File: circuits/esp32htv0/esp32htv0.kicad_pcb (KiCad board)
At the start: 2 copper layers, 60.5 x 69.3 mm, 39 parts, among them J1 Power, SW1 SW_Push, U1 LD1117S33TR_SOT223, U2 ESP32-WROOM-32UE, U3 BME280

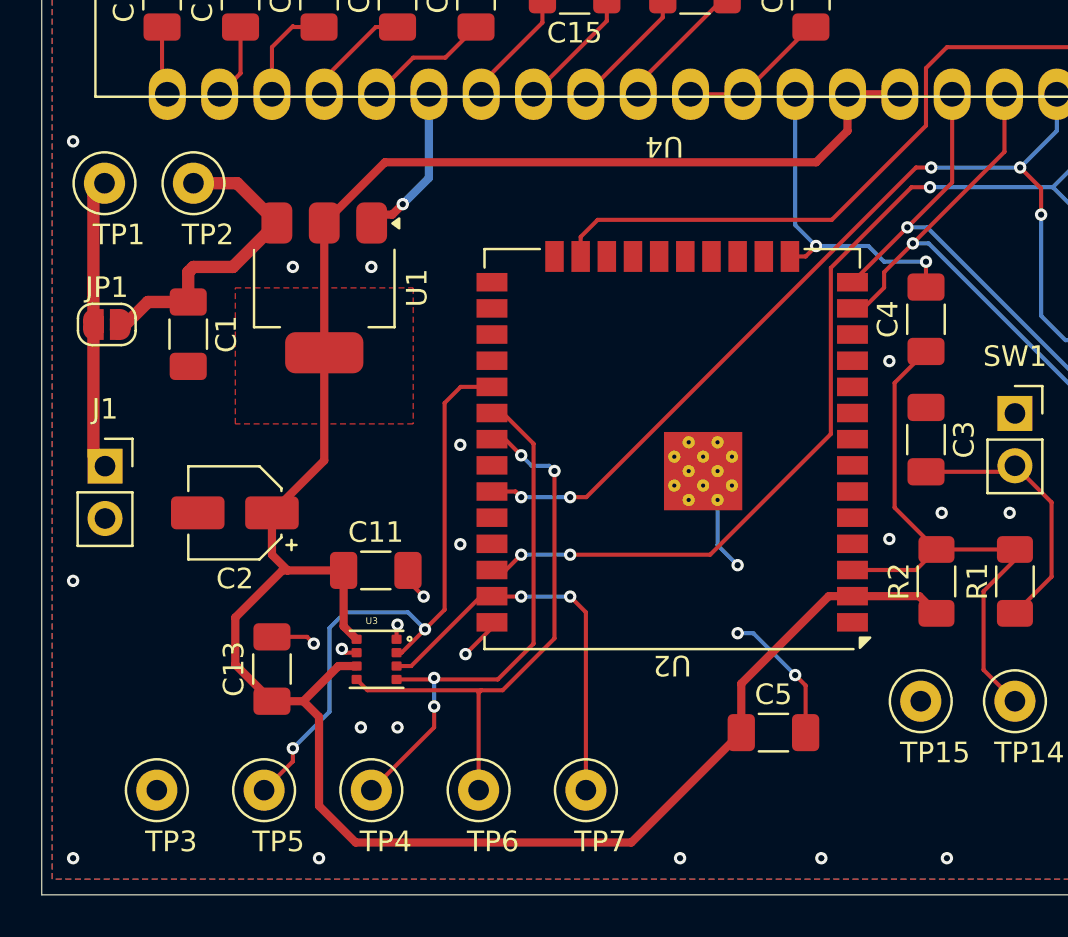
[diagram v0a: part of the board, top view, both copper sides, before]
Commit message: Updating the ESP32 with HTP concept circuit
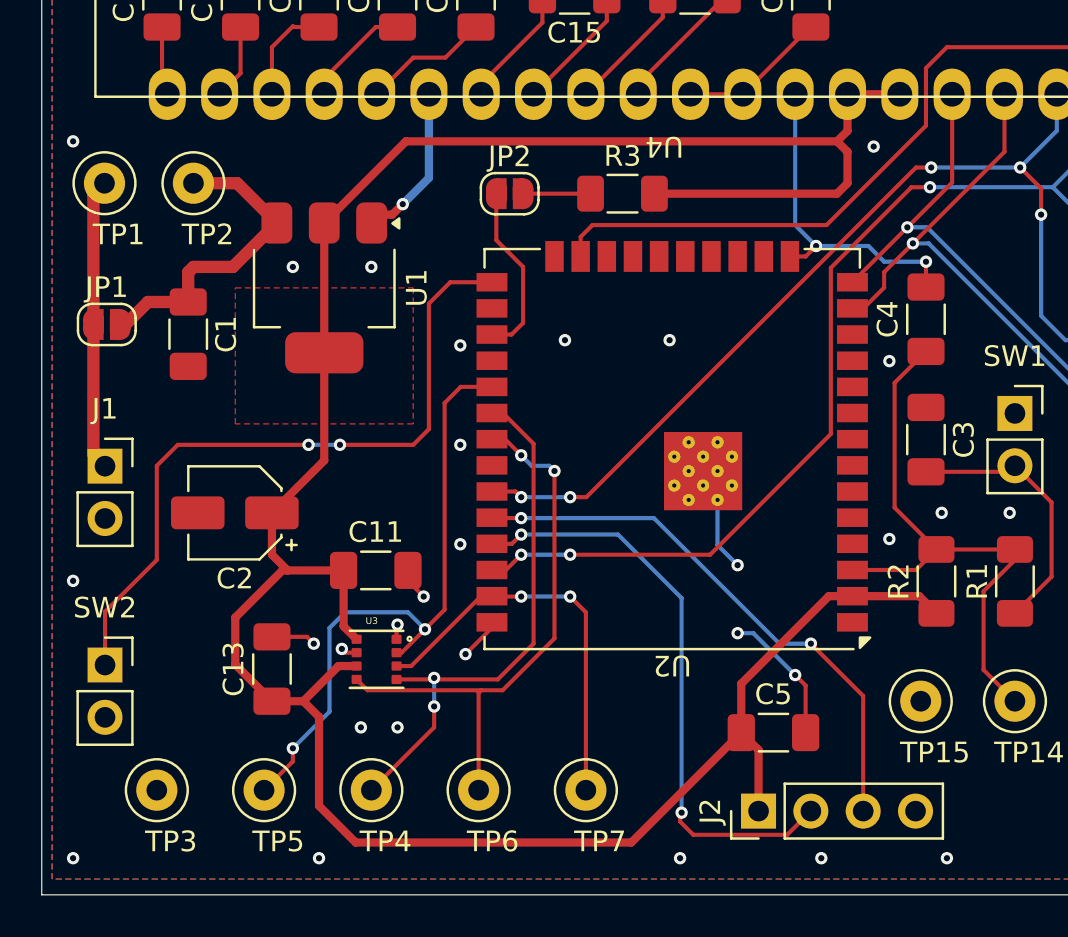
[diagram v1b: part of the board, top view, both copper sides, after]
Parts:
- added J2: UART, Connector_PinHeader_2.54mm:PinHeader_1x04_P2.54mm_Vertical, F.Cu at (155.2, 96.0)
- added JP2: ID_WP, Jumper:SolderJumper-2_P1.3mm_Open_RoundedPad1.0x1.5mm, F.Cu at (143.1, 66.0)
- added R3: 10k, Resistor_SMD:R_1206_3216Metric_Pad1.30x1.75mm_HandSolder, F.Cu at (148.6, 66.0)
- added SW2: BOOT, Connector_PinSocket_2.54mm:PinSocket_1x02_P2.54mm_Vertical, F.Cu at (123.5, 88.9)
- SW1: value SW_Push -> EN
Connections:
- U2 pad 25: unconnected-(U2-IO0-Pad25) -> Net-(U2-IO0)
- U2 pad 27: unconnected-(U2-IO16-Pad27) -> Net-(JP2-A)
- U2 pad 34: unconnected-(U2-RXD0/IO3-Pad34) -> Net-(J2-Pin_3)
- U2 pad 35: unconnected-(U2-TXD0/IO1-Pad35) -> Net-(J2-Pin_2)
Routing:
- net Net-(U2-IO0): track 0.00 -> 34.2 mm, vias 0 -> 2
- net Net-(J2-Pin_2): track 0.00 -> 28.7 mm, vias 0 -> 2
- net Net-(J2-Pin_3): track 0.00 -> 27.2 mm, vias 0 -> 2
- net +3V3: track 112.0 -> 128.3 mm
- net Net-(JP2-A): track 0.00 -> 8.56 mm
- net Net-(JP2-B): track 0.00 -> 3.28 mm
- net GND: vias 41 -> 45

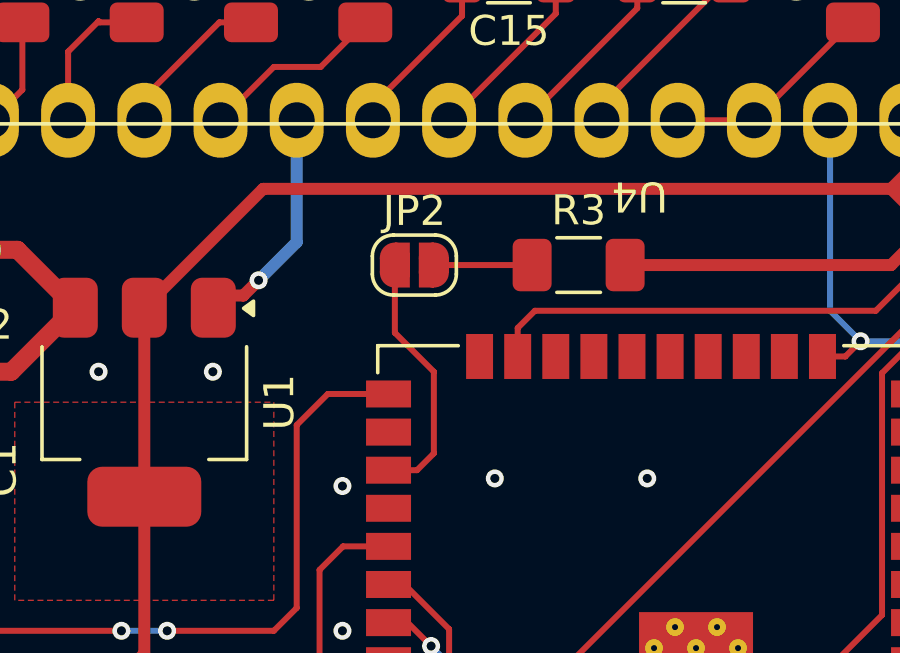
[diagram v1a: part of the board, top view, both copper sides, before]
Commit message: Updating the ESP32 HTV circuit and adding some documentation for display options
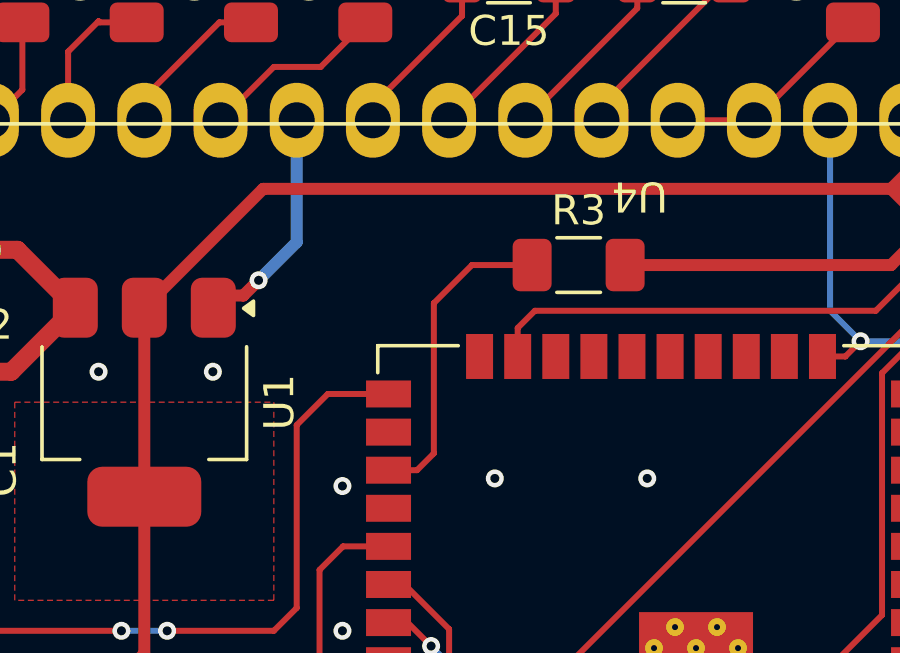
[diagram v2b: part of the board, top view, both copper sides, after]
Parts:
- removed JP2: ID_WP, Jumper:SolderJumper-2_P1.3mm_Open_RoundedPad1.0x1.5mm
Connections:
- R3 pad 1: Net-(JP2-B) -> Net-(U2-IO16)
- U2 pad 27: Net-(JP2-A) -> Net-(U2-IO16)
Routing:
- net Net-(U2-IO16): track 0.00 -> 10.6 mm
- net Net-(JP2-A): track 8.56 -> 0.00 mm
- net Net-(JP2-B): track 3.28 -> 0.00 mm

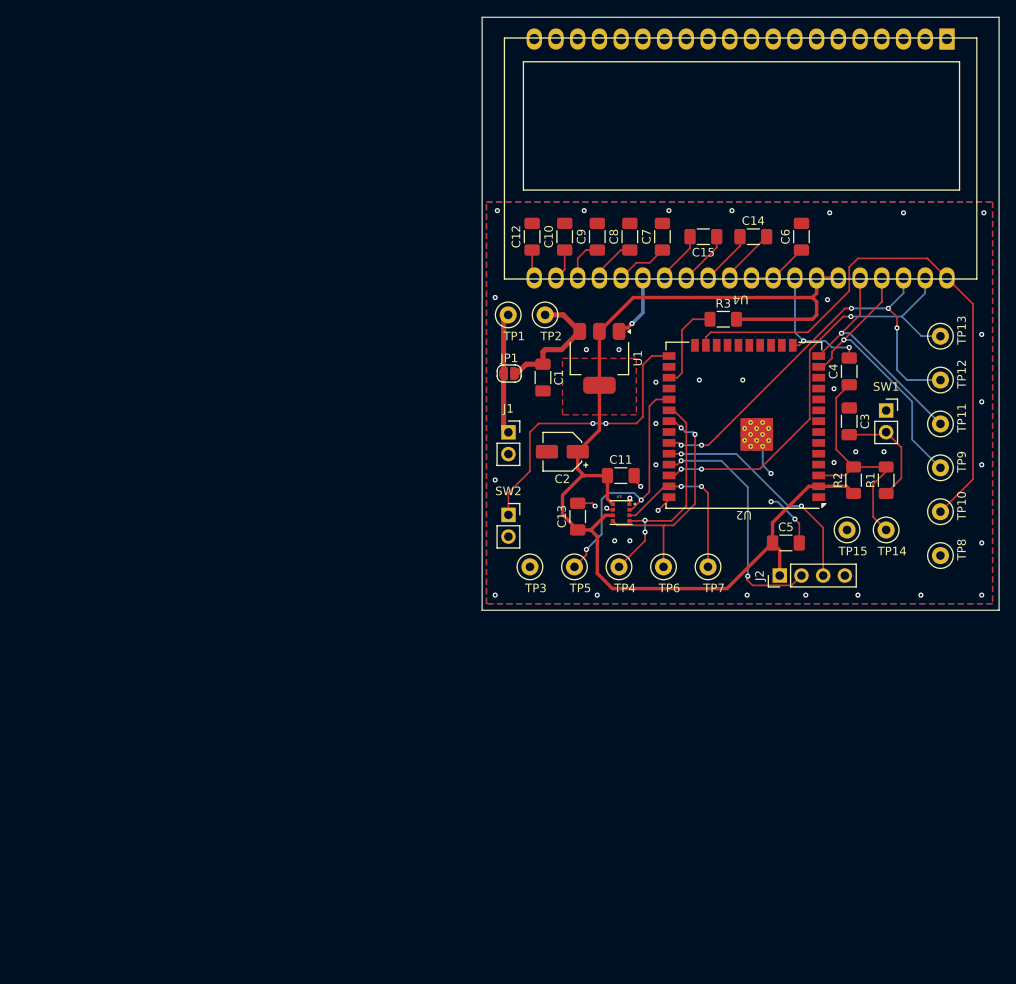
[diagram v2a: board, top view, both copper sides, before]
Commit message: Upgrade the ESP32 HTV prototype with DOGS102 display
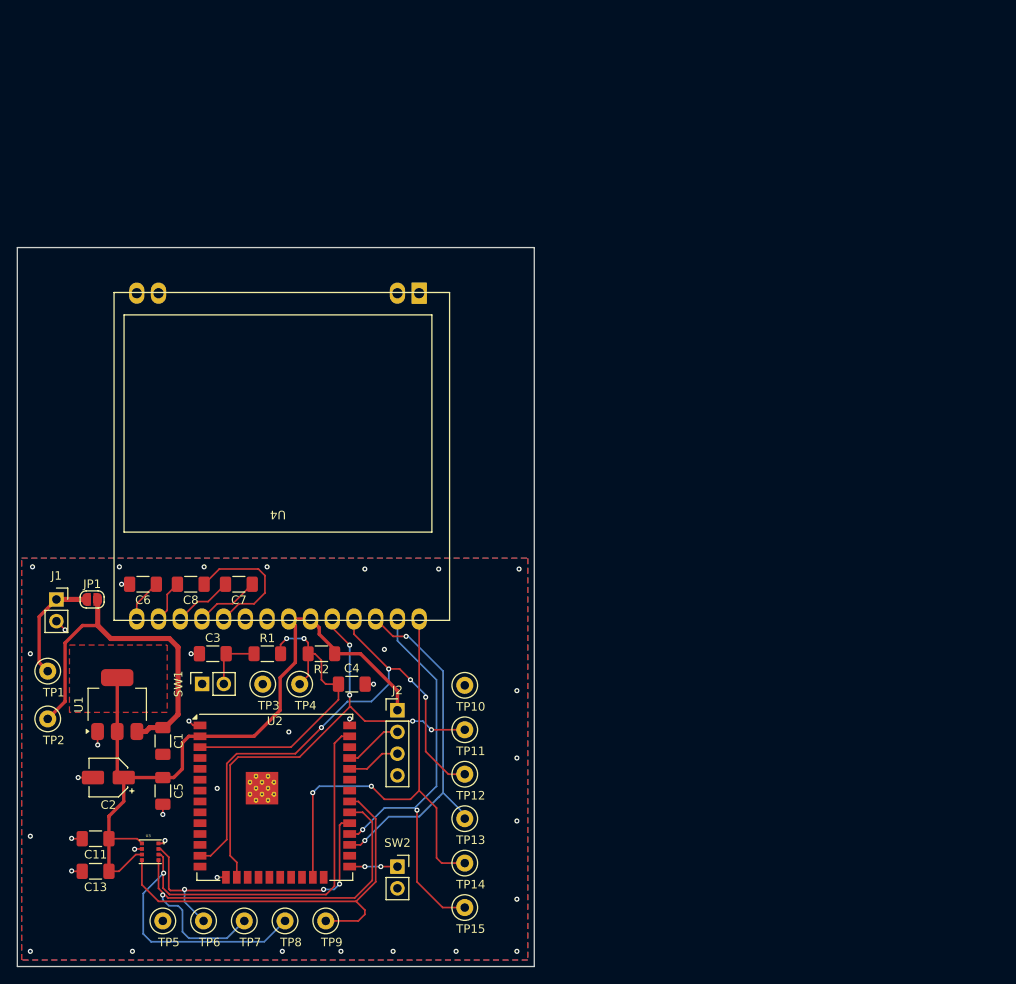
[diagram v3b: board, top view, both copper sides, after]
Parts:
- removed C10, C12, C14, C15, C9: 1 uF, Capacitor_SMD:C_1206_3216Metric_Pad1.33x1.80mm_HandSolder
- removed R3: 10k, Resistor_SMD:R_1206_3216Metric_Pad1.30x1.75mm_HandSolder
- TP10: value HSPI CS -> DOG GND
- TP11: value HSPI MISO -> DOG SDA
- TP12: value A0 -> DOG SCK
- TP13: value DISP RST -> DOG CD
- TP14: value EN -> DOG CS0
- TP15: value EN GND -> DOG RST
- TP3: value VSPI GND -> EN GND
- TP4: value VSPI CLK -> EN
- TP5: value VSPI CS -> BME GND
- TP6: value VSPI MISO -> BME CSB
- TP7: value VSPI MOSI -> BME SCK
- TP8: value HSPI GND -> BME SDI
- TP9: value HSPI CLK -> BME SDO
- U4: footprint gos:DOGM132-5 -> gos:DOGS102-6
- moved TP9 89.3 mm to (102.1, 136.4), turned to 0 degrees
- moved TP8 87.7 mm to (97.3, 136.4), turned to 0 degrees
- moved C6 87.1 mm to (80.7, 97.0), turned to 180 degrees
- moved SW1 86.1 mm to (87.7, 108.7), turned to 90 degrees
- moved TP13 79.2 mm to (118.4, 124.4), turned to 0 degrees
- moved C3 79.2 mm to (88.9, 105.2), turned to 0 degrees
- moved C5 78.4 mm to (83.1, 121.2), turned to -90 degrees
- moved R1 75.2 mm to (95.3, 105.2), turned to 0 degrees
- moved TP2 74.9 mm to (69.6, 112.8)
- moved C11 74.7 mm to (75.2, 126.8), turned to 180 degrees
- moved TP12 72.2 mm to (118.4, 119.2), turned to 0 degrees
- moved U2 70.0 mm to (96.2, 121.9), turned to 0 degrees
- moved C13 70.0 mm to (75.2, 130.6), turned to 180 degrees
- moved U1 69.4 mm to (77.7, 111.1), turned to 90 degrees
- moved C4 68.7 mm to (105.2, 108.7), turned to 0 degrees
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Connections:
- C6 pad 1: Net-(U4-CAP3P) -> Net-(U4-VLCD)
- C7 pad 1: Net-(U4-V4) -> Net-(U4-VB0+)
- C7 pad 2: GND -> Net-(U4-VB0-)
- C8 pad 1: Net-(U4-V3) -> Net-(U4-VB1+)
- C8 pad 2: GND -> Net-(U4-VB1-)
- TP10 pad 1: Net-(U2-IO15) -> GND
- TP11 pad 1: Net-(U2-IO12) -> Net-(U2-IO13)
- TP12 pad 1: Net-(U2-IO21) -> Net-(U2-IO14)
- TP13 pad 1: Net-(U2-IO22) -> Net-(U2-IO16)
- TP14 pad 1: Net-(U2-EN) -> Net-(U2-IO15)
- TP15 pad 1: GND -> Net-(U2-IO17)
- TP4 pad 1: Net-(U2-IO18) -> Net-(U2-EN)
- TP5 pad 1: Net-(U2-IO5) -> GND
- TP6 pad 1: Net-(U2-IO19) -> Net-(U2-IO5)
- TP7 pad 1: Net-(U2-IO23) -> Net-(U2-IO18)
- TP8 pad 1: GND -> Net-(U2-IO23)
- TP9 pad 1: Net-(U2-IO14) -> Net-(U2-IO19)
- U2 pad 14: Net-(U2-IO12) -> unconnected-(U2-IO12-Pad14)
- U2 pad 16: unconnected-(U2-IO13-Pad16) -> Net-(U2-IO13)
- U2 pad 28: unconnected-(U2-IO17-Pad28) -> Net-(U2-IO17)
- U2 pad 33: Net-(U2-IO21) -> unconnected-(U2-IO21-Pad33)
- U2 pad 36: Net-(U2-IO22) -> unconnected-(U2-IO22-Pad36)
- U4 pad 15: (no net) -> Net-(U4-VLCD)
- U4 pad 16: (no net) -> Net-(U4-VB1-)
- U4 pad 17: (no net) -> Net-(U4-VB0-)
- U4 pad 18: (no net) -> Net-(U4-VB0+)
- U4 pad 19: (no net) -> Net-(U4-VB1+)
- U4 pad 20: (no net) -> GND
- U4 pad 21: Net-(U4-V0) -> GND
- U4 pad 22: Net-(U4-V1) -> +3V3
- U4 pad 23: Net-(U4-V2) -> +3V3
- U4 pad 24: Net-(U4-V3) -> Net-(U2-IO13)
- U4 pad 25: Net-(U4-V4) -> Net-(U2-IO14)
- U4 pad 26: GND -> Net-(U2-IO16)
- U4 pad 27: Net-(U4-CAP2N) -> Net-(U2-IO17)
- U4 pad 28: Net-(U4-CAP2P) -> Net-(U2-IO15)
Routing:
- net Net-(U2-IO13): track 0.00 -> 55.9 mm, vias 0 -> 4
- net Net-(U2-IO22): track 50.8 -> 0.00 mm, vias 3 -> 0
- net Net-(U2-IO23): track 19.6 -> 69.9 mm, vias 2 -> 1
- net Net-(U2-IO21): track 49.9 -> 0.00 mm, vias 5 -> 0
- net Net-(U2-IO17): track 0.00 -> 49.5 mm, vias 0 -> 2
- net +3V3: track 128.3 -> 86.7 mm
- net Net-(U2-IO16): track 10.6 -> 42.2 mm, vias 0 -> 2
- net Net-(U2-IO14): track 33.8 -> 62.8 mm, vias 1 -> 4
- net Net-(U2-IO0): track 34.2 -> 5.59 mm
- net Net-(U2-IO18): track 26.4 -> 53.9 mm, vias 2 -> 1
- net Net-(U2-IO12): track 27.1 -> 0.00 mm, vias 1 -> 0
- net +5V: track 15.3 -> 41.4 mm
- net GND: track 41.5 -> 16.4 mm, vias 45 -> 37
- net Net-(U2-IO19): track 27.6 -> 50.1 mm, vias 2 -> 0
- net Net-(J2-Pin_2): track 28.7 -> 6.85 mm, vias 2 -> 0
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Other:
- board size 60.5 x 69.3 mm -> 60.5 x 84.1 mm
